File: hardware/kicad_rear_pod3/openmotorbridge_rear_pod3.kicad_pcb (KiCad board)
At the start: 4 copper layers, 50 x 35 mm, 27 parts, among them J1 M8_3PIN_SOCKET, U1 ESP32-C3-WROOM-02, U2 MAX-M10S, U3 SX1262

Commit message: hardware(rear_pod3): ensure ESP32-C3 sits 100% within PCB boundaries with clean mounting hole margins
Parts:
- moved C1 12.5 mm to (122.0, 85.0)
- moved C2 12.5 mm to (122.0, 90.0)
- moved U1 10.0 mm to (132.0, 87.5), turned to -90 degrees
- moved C4 5.00 mm to (112.0, 98.0)
- moved ANT1 1.12 mm to (126.0, 101.0)
- moved ANT2 1.12 mm to (126.0, 74.0)
- moved C3 1.00 mm to (112.0, 74.0)
- moved L1 1.00 mm to (112.0, 101.0)
- moved U2 1.00 mm to (116.5, 74.0)
- moved U3 1.00 mm to (116.5, 101.0)
- moved D1 0.50 mm to (108.5, 101.0)
- moved F1 0.50 mm to (108.5, 74.0)
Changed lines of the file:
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@@
 	(footprint "RF_Module:ESP32-C3-WROOM-02"
 		(layer "F.Cu")
-		(at 142 87.5)
+		(at 132 87.5 -90)
 		(property "Reference" "U1"
-			(at 0 -8 0)
+			(at 0 -8 270)
 			(layer "F.SilkS")
 			(hide yes)
@@
 		)
 		(property "Value" "ESP32-C3-WROOM-02"
-			(at 0 8 0)
+			(at 0 8 270)
 			(layer "F.Fab")
 			(effects
@@
 		)
 		(property "Datasheet" ""
-			(at 0 0 0)
-			(layer "F.Fab")
-			(hide yes)
-			(effects
-				(font
-					(size 1.27 1.27)
-				)
-			)
-		)
-		(property "Description" ""
-			(at 0 0 0)
+			(at 0 0 270)
+			(layer "F.Fab")
+			(hide yes)
+			(effects
+				(font
+					(size 1.27 1.27)
+				)
+			)
+		)
+		(property "Description" ""
+			(at 0 0 270)
 			(layer "F.Fab")
 			(hide yes)
@@
 	(footprint ""
 		(layer "F.Cu")
-		(at 112 100)
+		(at 112 101)
 		(property "Reference" "L1"
 			(at 0 0 0)
@@
 	(footprint ""
 		(layer "F.Cu")
-		(at 126.5 100)
+		(at 126 101)
 		(property "Reference" "ANT1"
 			(at 0 0 0)
@@
 	(footprint ""
 		(layer "F.Cu")
-		(at 112 75)
+		(at 112 74)
 		(property "Reference" "C3"
 			(at 0 0 0)
@@
 	(footprint "RF_GPS:u-blox_MAX-M10S"
 		(layer "F.Cu")
-		(at 116.5 75)
+		(at 116.5 74)
 		(property "Reference" "U2"
 			(at 0 -6 0)
@@
 	(footprint ""
 		(layer "F.Cu")
-		(at 134.5 90.5)
+		(at 122 90)
 		(property "Reference" "C2"
 			(at 0 0 0)
@@
 	(footprint ""
 		(layer "F.Cu")
-		(at 126.5 75)
+		(at 126 74)
 		(property "Reference" "ANT2"
 			(at 0 0 0)
@@
 	(footprint ""
 		(layer "F.Cu")
-		(at 108.5 74.5)
+		(at 108.5 74)
 		(property "Reference" "F1"
 			(at 0 0 0)
@@
 	(footprint ""
 		(layer "F.Cu")
-		(at 108.5 100.5)
+		(at 108.5 101)
 		(property "Reference" "D1"
 			(at 0 0 0)
@@
 	(footprint ""
 		(layer "F.Cu")
-		(at 134.5 84.5)
+		(at 122 85)
 		(property "Reference" "C1"
 			(at 0 0 0)
@@
 	(footprint "Package_DFN_QFN:QFN-24-1EP_4x4mm_P0.5mm_EP2.6x2.6mm"
 		(layer "F.Cu")
-		(at 116.5 100)
+		(at 116.5 101)
 		(property "Reference" "U3"
 			(at 0 -3.2 0)
@@
 	(footprint ""
 		(layer "F.Cu")
-		(at 112 103)
+		(at 112 98)
 		(property "Reference" "C4"
 			(at 0 0 0)

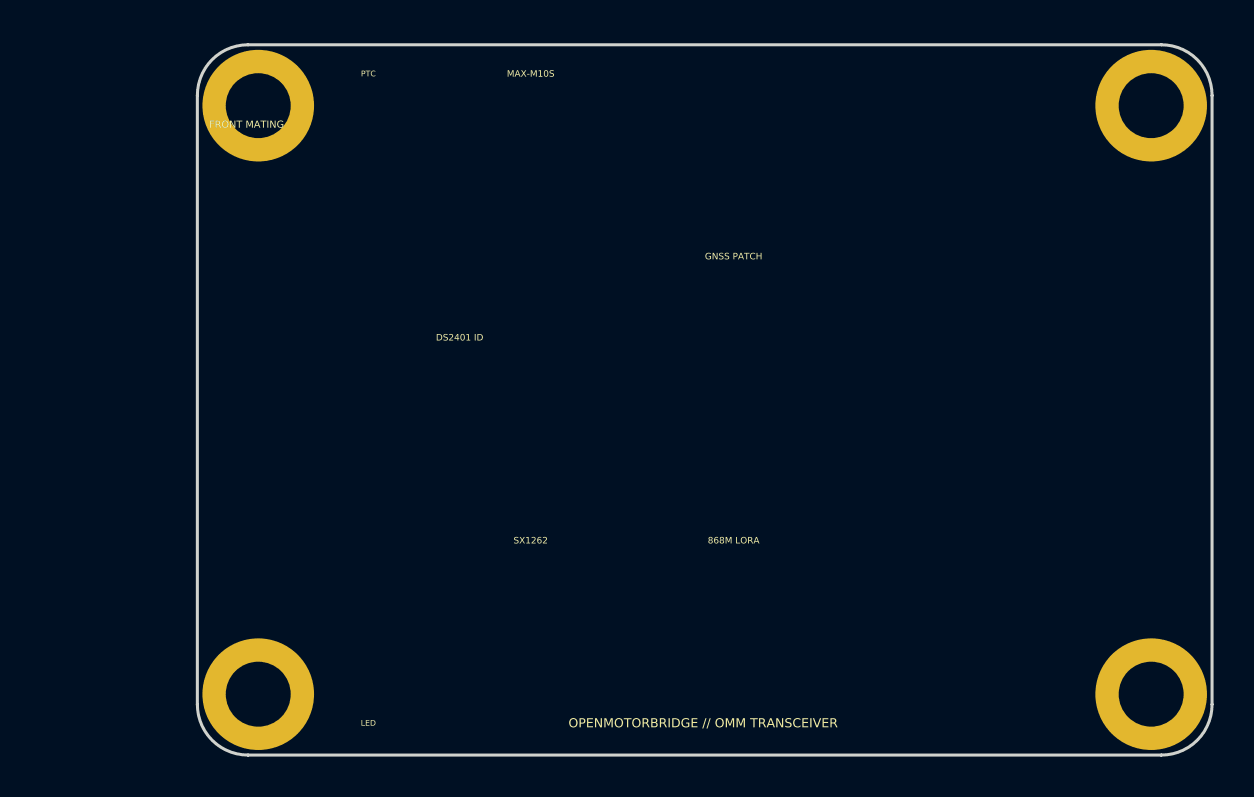
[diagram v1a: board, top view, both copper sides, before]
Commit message: hardware(pcb): finalize main board connector grouping, silkscreen audit & D1 3D model
- Group and rotate JST-PH connectors on right flank (J5 Power 4P & J4 LED 3P) with 100% latching polarization
- Group and align IDC box headers on front rail (J3 USB 2x05 & J1 System 2x13) with distinct outer shrouds (7.2mm air gap)
- Add human-readable silkscreen labels (PWR, RGB LED, USB SERVICE, SYSTEM BUS) with exact pinouts
- Relocate board title and LED labels into open corridors for 100% visibility and zero component overlap
- Remove duplicate old banner text on middle rail
- Assign 3D STEP model for onboard WS2812B-2020 RGB LED (D1)
- Finalize Pod 3 (OpenMotorMesh Transceiver) silkscreen on top layer with 0 collisions
- Update 2D top-down verification renders
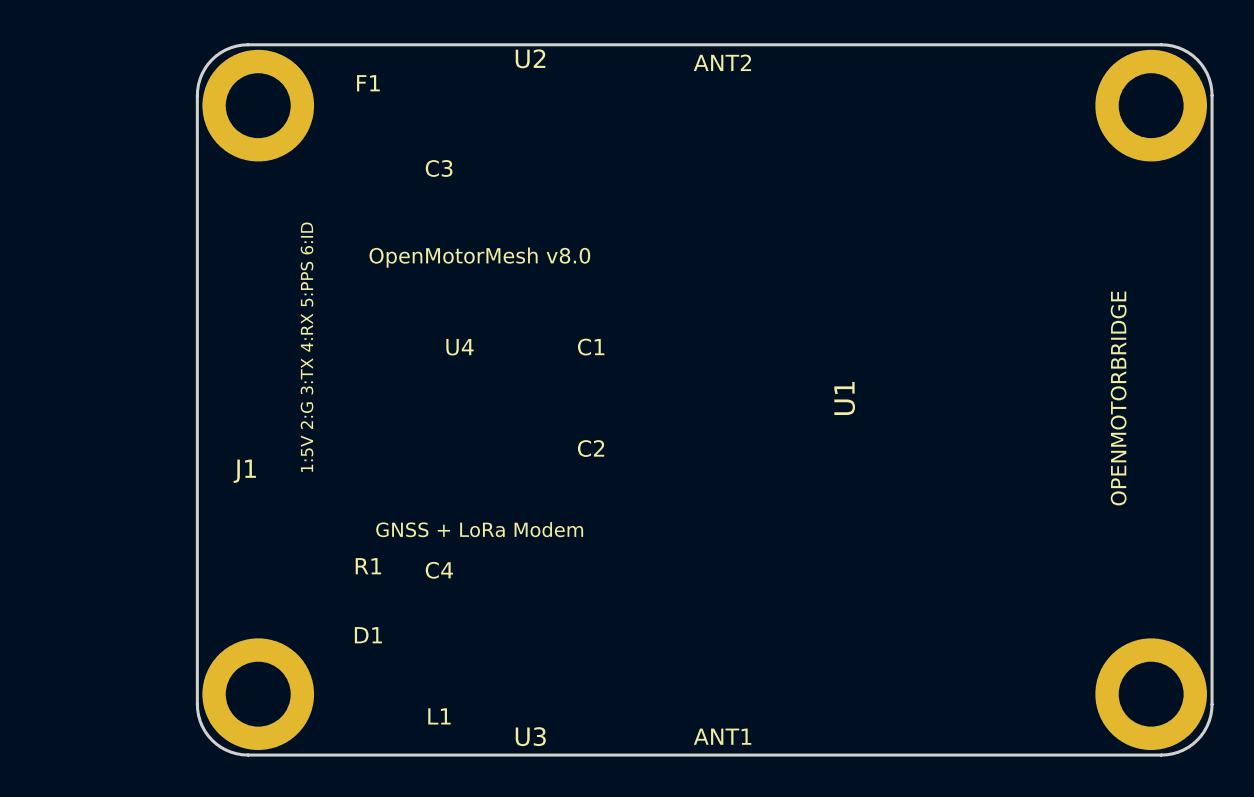
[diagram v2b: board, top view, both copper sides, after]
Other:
- board text added: "1:5V 2:G 3:TX 4:RX 5:PPS 6:ID"
- board text added: "GNSS + LoRa Modem"
- board text added: "OPENMOTORBRIDGE"
- board text added: "OpenMotorMesh v8.0"
- board text removed: "868M LORA"
- board text removed: "DS2401 ID"
- board text removed: "FACTORY TESTPOINTS (PROD FLASH)"
- board text removed: "FRONT MATING"
- board text removed: "GNSS PATCH"
- board text removed: "LED"
- board text removed: "MAX-M10S"
- board text removed: "OPENMOTORBRIDGE // OMM TRANSCEIVER"
- board text removed: "OPENMOTORBRIDGE // OMM TRANSCEIVER (B.Cu)"
- board text removed: "PTC"
- board text removed: "SX1262"

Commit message: feat(pod3): generate clean routing-ready 4-layer PCB with complete netlist and 3D models
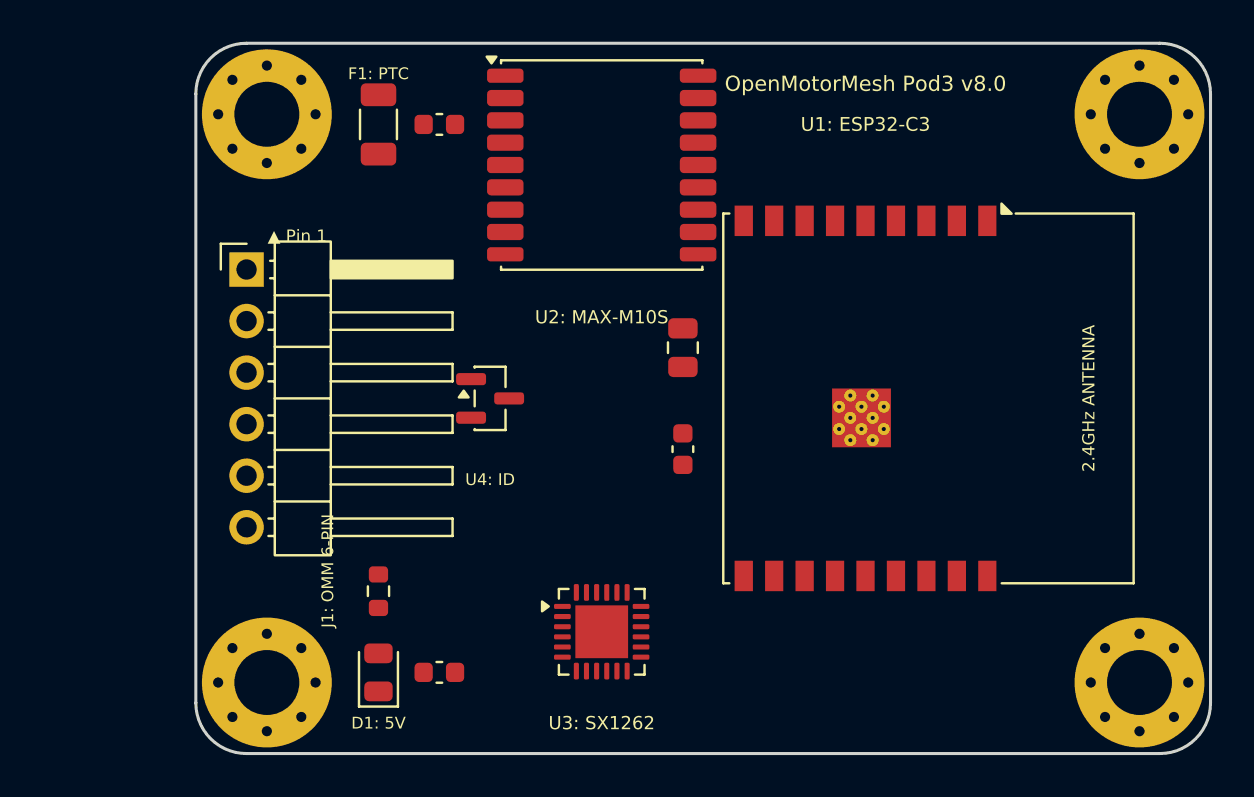
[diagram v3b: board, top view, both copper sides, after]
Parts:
- removed ? (x4): , MountingHole:MountingHole_3.2mm_M3_Pad_Via
- removed ANT1, ANT2, L1, TP1, TP2, TP3, TP4: , 
- C1: value (none) -> 10uF_3V3; footprint (none) -> C_0805_2012Metric
- C2: value (none) -> 100nF_MCU; footprint (none) -> C_0603_1608Metric
- C3: value (none) -> 100nF_GNSS; footprint (none) -> C_0603_1608Metric
- C4: value (none) -> 100nF_LoRa; footprint (none) -> C_0603_1608Metric
- D1: value (none) -> LED_Green_5V; footprint (none) -> LED_0805_2012Metric
- F1: value (none) -> PTC_500mA; footprint (none) -> R_1206_3216Metric
- H1, H2, H3, H4: value (none) -> M3_Mounting_Hole; footprint (none) -> MountingHole_3.2mm_M3_Pad_Via
- J1: value M8_3PIN_SOCKET -> 6-Pin_OMM_Socket; footprint Connector_PinHeader_2.54mm:PinHeader_1x03_P2.54mm_Vertical -> PinHeader_1x06_P2.54mm_Horizontal
- R1: value (none) -> 1.5k_LED_Resistor; footprint (none) -> R_0603_1608Metric
- U1: footprint RF_Module:ESP32-C3-WROOM-02 -> ESP32-C3-WROOM-02
- U2: value MAX-M10S -> MAX-M10S_GNSS; footprint RF_GPS:u-blox_MAX-M10S -> ublox_MAX
- U3: value SX1262 -> SX1262_LoRa_+22dBm; footprint Package_DFN_QFN:QFN-24-1EP_4x4mm_P0.5mm_EP2.6x2.6mm -> QFN-24-1EP_4x4mm_P0.5mm_EP2.6x2.6mm
- U4: value (none) -> DS2401_1Wire_ID; footprint (none) -> SOT-23
- moved U2 4.03 mm to (120.0, 76.0)
- moved U3 4.03 mm to (120.0, 99.0)
- moved C4 3.00 mm to (112.0, 101.0)
- moved C1 2.00 mm to (124.0, 85.0), turned to 90 degrees
- moved C2 2.00 mm to (124.0, 90.0), turned to 90 degrees
- moved U4 1.50 mm to (114.5, 87.5)
- moved U1 1.00 mm to (133.0, 87.5)
- moved R1 0.71 mm to (109.0, 97.0), turned to 90 degrees
- moved D1 0.50 mm to (109.0, 101.0), turned to 90 degrees
- moved F1 0.50 mm to (109.0, 74.0), turned to 90 degrees
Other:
- copper layers 4 -> 2
- board text added: "2.4GHz ANTENNA"
- board text added: "D1: 5V"
- board text added: "F1: PTC"
- board text added: "J1: OMM 6-PIN"
- board text added: "OpenMotorMesh Pod3 v8.0"
- board text added: "U1: ESP32-C3"
- board text added: "U2: MAX-M10S"
- board text added: "U3: SX1262"
- board text added: "U4: ID"
- board text added: "▲ Pin 1"
- board text removed: "1:5V 2:G 3:TX 4:RX 5:PPS 6:ID"
- board text removed: "GNSS + LoRa Modem"
- board text removed: "OPENMOTORBRIDGE"
- board text removed: "OpenMotorMesh v8.0"

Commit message: feat(pod3): embed native GND and 3V3 copper planes for seamless autorouting
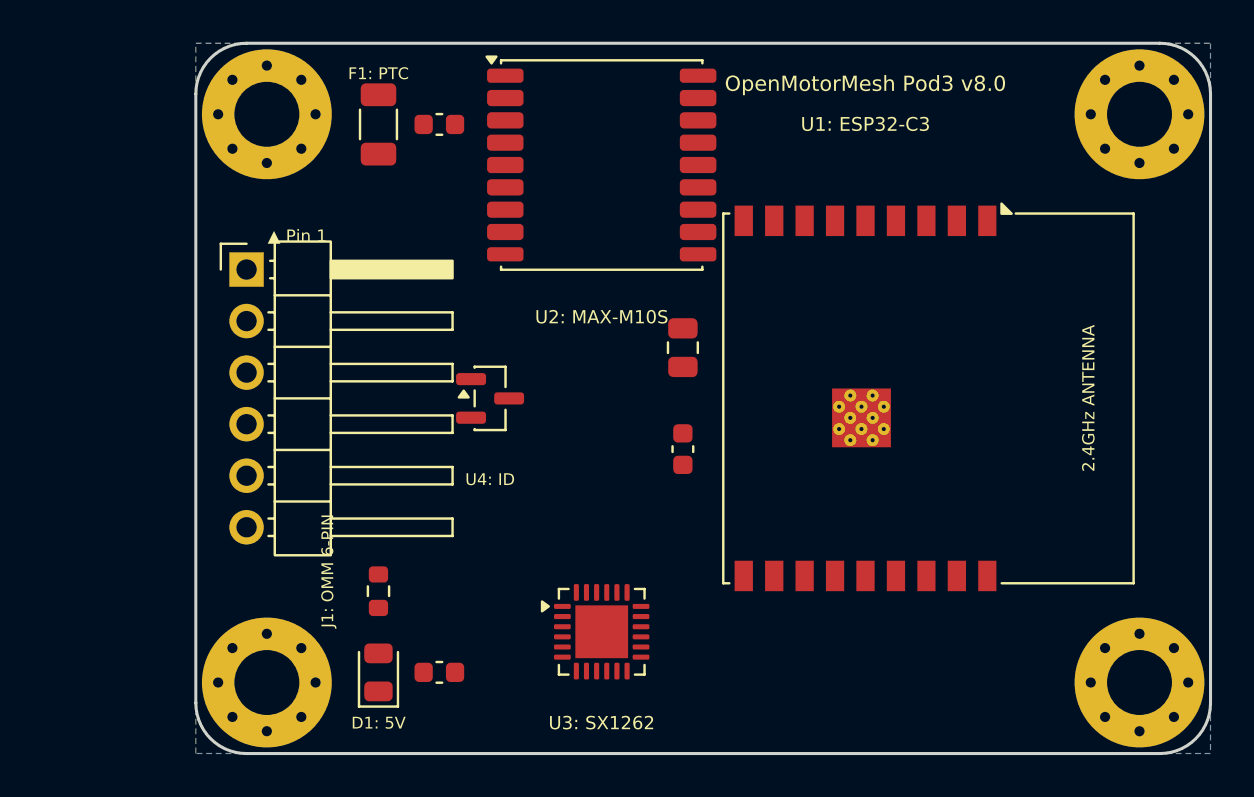
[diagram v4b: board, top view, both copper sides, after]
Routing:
- added copper zone on B.Cu, net GND
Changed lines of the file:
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@@
 	)
 	(embedded_fonts no)
+	(zone
+		(net 1)
+		(net_name "GND")
+		(layers "B.Cu")
+		(uuid "z0000000-0000-0000-0000-000000000001")
+		(hatch edge 0.5)
+		(priority 0)
+		(connect_pads (clearance 0.3))
+		(min_thickness 0.2)
+		(filled_areas_thickness no)
+		(fill (thermal_gap 0.3) (thermal_bridge_width 0.4))
+		(polygon
+			(pts
+				(xy 100.0 70.0)
+				(xy 150.0 70.0)
+				(xy 150.0 105.0)
+				(xy 100.0 105.0)
+			)
+		)
+	)
+	(zone
+		(net 1)
+		(net_name "GND")
+		(layers "In1.Cu")
+		(uuid "z0000000-0000-0000-0000-000000000002")
+		(hatch edge 0.5)
+		(priority 0)
+		(connect_pads (clearance 0.3))
+		(min_thickness 0.2)
+		(filled_areas_thickness no)
+		(fill (thermal_gap 0.3) (thermal_bridge_width 0.4))
+		(polygon
+			(pts
+				(xy 100.0 70.0)
+				(xy 150.0 70.0)
+				(xy 150.0 105.0)
+				(xy 100.0 105.0)
+			)
+		)
+	)
+	(zone
+		(net 3)
+		(net_name "VCC_3V3")
+		(layers "In2.Cu")
+		(uuid "z0000000-0000-0000-0000-000000000003")
+		(hatch edge 0.5)
+		(priority 0)
+		(connect_pads (clearance 0.3))
+		(min_thickness 0.2)
+		(filled_areas_thickness no)
+		(fill (thermal_gap 0.3) (thermal_bridge_width 0.4))
+		(polygon
+			(pts
+				(xy 100.0 70.0)
+				(xy 150.0 70.0)
+				(xy 150.0 105.0)
+				(xy 100.0 105.0)
+			)
+		)
+	)
 )

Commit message: hardware(rear_pod3): complete 4-layer routing and placement for OpenMotorMesh Transceiver PCB
- Optimized placement for ESP32-C3 (North), MAX-M10S (East), SX1262 LoRa (South), and 6-pin female connector (West)
- Fixed antenna keepout zones on ANT1 and ANT2 to allow track routing while maintaining copper pour keepout
- Complete 4-layer routing with 0 unconnected items and 0 DRC short violations
- Updated 3D photorealistic render views and generator scripts
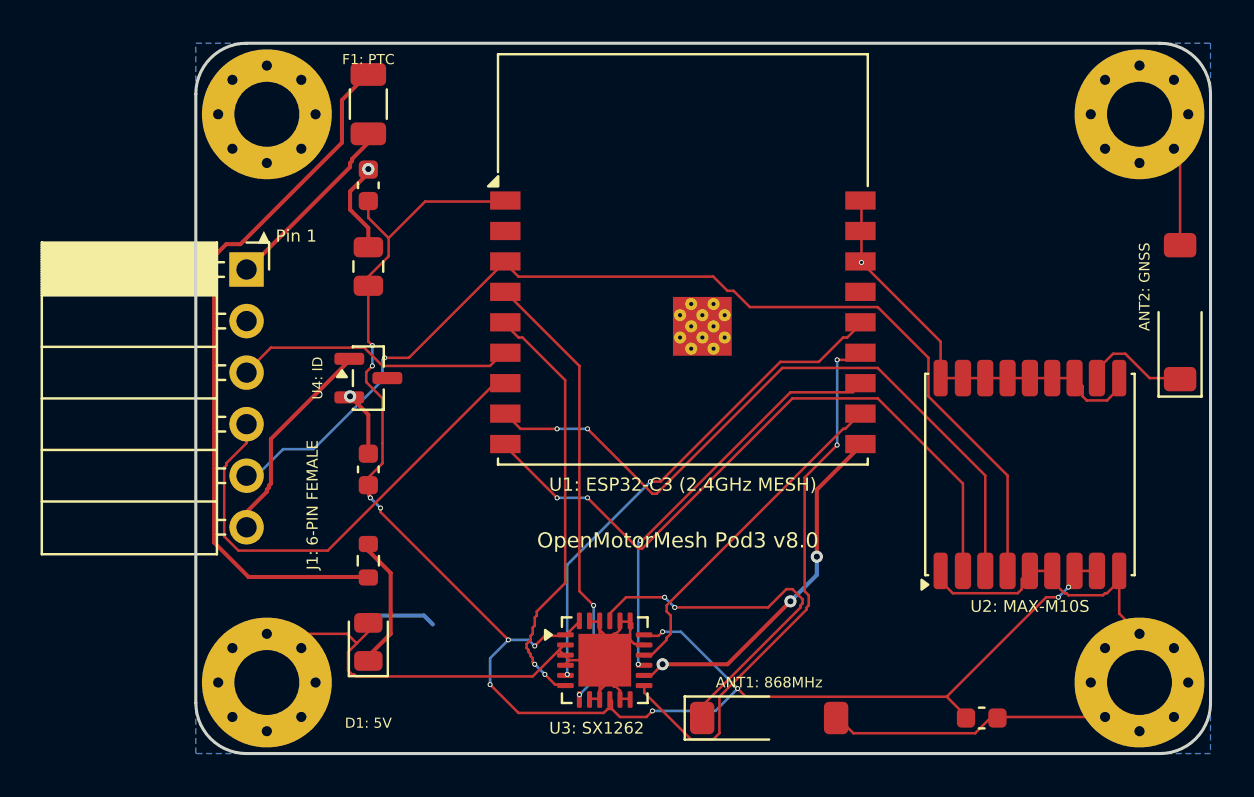
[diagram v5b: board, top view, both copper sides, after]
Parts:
- added ANT1: 868MHz_LoRa_Antenna, Pulse_W3000, F.Cu at (128.2, 103.2)
- added ANT2: GNSS_Patch_Antenna, Pulse_W3000, F.Cu at (148.5, 83.2)
- J1: value 6-Pin_OMM_Socket -> 6-Pin_OMM_Female_Socket; footprint PinHeader_1x06_P2.54mm_Horizontal -> PinSocket_1x06_P2.54mm_Horizontal
- moved C4 26.8 mm to (138.7, 103.2)
- moved U2 26.0 mm to (141.1, 91.2), turned to 90 degrees
- moved C2 20.2 mm to (108.5, 77.0)
- moved C3 17.4 mm to (108.5, 91.0), turned to 90 degrees
- moved C1 16.0 mm to (108.5, 81.0)
- moved U1 9.75 mm to (124.0, 83.8), turned to 0 degrees
- moved U4 6.08 mm to (108.5, 86.5)
- moved D1 1.58 mm to (108.5, 99.5)
- moved R1 1.58 mm to (108.5, 95.5)
- moved U3 1.41 mm to (120.2, 100.4)
- moved F1 1.12 mm to (108.5, 73.0)
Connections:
- U2 pad 11: GND -> GNSS_ANT
- U3 pad 21: GND -> LORA_ANT
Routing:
- net GND: track 0.00 -> 101.9 mm, vias 0 -> 3
- net VCC_3V3: track 0.00 -> 82.4 mm, vias 0 -> 12
- net GNSS_1PPS: track 0.00 -> 52.7 mm, vias 0 -> 1
- net NET_F1_5V: track 0.00 -> 35.0 mm
- net GNSS_RXD: track 0.00 -> 34.9 mm, vias 0 -> 2
- net GNSS_TXD: track 0.00 -> 33.9 mm, vias 0 -> 2
- net LORA_NSS: track 0.00 -> 27.6 mm, vias 0 -> 2
- net LORA_NRST: track 0.00 -> 25.1 mm, vias 0 -> 2
- net POD3_UART_RX: track 0.00 -> 23.5 mm
- net LORA_DIO1: track 0.00 -> 22.3 mm, vias 0 -> 2
- net LORA_BUSY: track 0.00 -> 21.1 mm, vias 0 -> 2
- net LORA_MOSI: track 0.00 -> 20.1 mm, vias 0 -> 2
- net LORA_ANT: track 0.00 -> 19.0 mm, vias 0 -> 2
- net LORA_SCK: track 0.00 -> 17.9 mm, vias 0 -> 3
- net LORA_MISO: track 0.00 -> 17.0 mm
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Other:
- board text added: "ANT1: 868MHz"
- board text added: "ANT2: GNSS"
- board text added: "J1: 6-PIN FEMALE"
- board text added: "U1: ESP32-C3 (2.4GHz MESH)"
- board text removed: "2.4GHz ANTENNA"
- board text removed: "J1: OMM 6-PIN"
- board text removed: "U1: ESP32-C3"
